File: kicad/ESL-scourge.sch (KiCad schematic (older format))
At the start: 39 parts, among them IC1 MOC3020M, J1 DB9, J2 DB9, P1 CONN_4, P2 CONN_3, P3 CONN_4, Q1 NPN, Q2 NPN, Q3 NPN, U1 TDA2030

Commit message: Comments for debugging added
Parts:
- C6: value 1.0 -> 1.0 x 250V
- D1, D10, D2, D3, D4, D6, D7, D8, D9: value DIODE -> SMA4007 (GS1M)
- Q1, Q2, Q3: value NPN -> BC847
- R10: value R -> 0*
- R8: value R -> 1M*
- R9: value R -> 2k*
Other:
- note added: "*"
- note added: "12V"
- note added: "220V"
- note added: "R1 и R2 подбираются так, чтобы\nАМПЛИТУДНОЕ выходное\nнапряжение менялось в диапазоне\nне менее, чем 20-100 В.\nС помощью осциллографа с\nделителем убедиться, что\nсинус на выходе не срезается."
- note added: "R6=(Vcc-4)/0,015, округляется в\nсторону уменьшения до близжайшего\nдоступного номинала, но не менее,\nчем (Vcc-2)/0,05\n"
- note added: "Если вольтметр на 150В:\nR10 - 0 ом (перемычка)\nR8 - 1M или не монтировать вообще\n(посмотреть, насколько бодро\nвольтметр реагирует на вращение\nрегулятора напряжения)."
- note added: "Здесь важна фазировка обмоток:\nнапряжения должны суммироваться,\nа не вычитаться. Необходимо\nизмерить переменное напряжение\nмежду выводами 1 и 4 P1\n - если там 24 В - все ОК\n - если там около нуля, необходимо\nпоменять местами концы одной из\nвторичных обмоток.\nПредварительно надо убедиться,\nчто на каждой из обмоток есть 12 В."
- note added: "По умолчанию установлен (замкнут)"
- note added: "Посмотреть выходной сигнал\nс отключенным демпфером (R5C5).\nЕсли все ОК - демпфер не ставить."
- note added: "для подбора R9 сделать следующее:\nпри максимальном напряжении на\nвыходе замкнуть контакты 7 и 8\nили лучше замкнуть контакт 8 с\nножкой 6 IC1. Если напряжение на\nвольтметре карабаса уменьшилось\nнезначительно - ОК."
- note added: "может быть заменить на КМОП-логику?"
- note added: "может быть стоит подключить\nвольтметр до резистора тк мб кз\nили предусмотреть индикацию КЗ?"
- note removed: "может быть заменить на КМОП-логику"
- note removed: "может быть стоит подключиться до резистора тк мб кз"
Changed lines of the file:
@@
 Sheet 1 1
 Title ""
-Date "14 feb 2016"
+Date "1 apr 2016"
 Rev ""
 Comp ""
@@
 P 5900 3250
 F 0 "D3" H 5900 3350 40  0000 C CNN
-F 1 "DIODE" H 5900 3150 40  0000 C CNN
+F 1 "SMA4007 (GS1M)" H 5900 3150 40  0000 C CNN
 F 2 "~" H 5900 3250 60  0000 C CNN
 F 3 "~" H 5900 3250 60  0000 C CNN
@@
 P 5900 3850
 F 0 "D4" H 5900 3950 40  0000 C CNN
-F 1 "DIODE" H 5900 3750 40  0000 C CNN
+F 1 "SMA4007 (GS1M)" H 5900 3750 40  0000 C CNN
 F 2 "~" H 5900 3850 60  0000 C CNN
 F 3 "~" H 5900 3850 60  0000 C CNN
@@
 P 8150 2450
 F 0 "C6" H 8150 2550 40  0000 L CNN
-F 1 "1.0" H 8156 2365 40  0000 L CNN
+F 1 "1.0 x 250V" H 8156 2365 40  0000 L CNN
 F 2 "~" H 8188 2300 30  0000 C CNN
 F 3 "~" H 8150 2450 60  0000 C CNN
@@
 P 2700 3000
 F 0 "D1" H 2700 3100 40  0000 C CNN
-F 1 "DIODE" H 2700 2900 40  0000 C CNN
+F 1 "SMA4007 (GS1M)" H 2700 2900 40  0000 C CNN
 F 2 "~" H 2700 3000 60  0000 C CNN
 F 3 "~" H 2700 3000 60  0000 C CNN
@@
 P 2700 3800
 F 0 "D2" H 2700 3900 40  0000 C CNN
-F 1 "DIODE" H 2700 3700 40  0000 C CNN
+F 1 "SMA4007 (GS1M)" H 2700 3700 40  0000 C CNN
 F 2 "~" H 2700 3800 60  0000 C CNN
 F 3 "~" H 2700 3800 60  0000 C CNN
@@
 P 9000 3550
 F 0 "D7" H 9000 3650 40  0000 C CNN
-F 1 "DIODE" H 9000 3450 40  0000 C CNN
+F 1 "SMA4007 (GS1M)" H 9000 3450 40  0000 C CNN
 F 2 "~" H 9000 3550 60  0000 C CNN
 F 3 "~" H 9000 3550 60  0000 C CNN
@@
 P 8300 3550
 F 0 "R9" V 8380 3550 40  0000 C CNN
-F 1 "R" V 8307 3551 40  0000 C CNN
+F 1 "2k*" V 8307 3551 40  0000 C CNN
 F 2 "~" V 8230 3550 30  0000 C CNN
 F 3 "~" H 8300 3550 30  0000 C CNN
@@
 P 9000 4150
 F 0 "D9" H 9000 4250 40  0000 C CNN
-F 1 "DIODE" H 9000 4050 40  0000 C CNN
+F 1 "SMA4007 (GS1M)" H 9000 4050 40  0000 C CNN
 F 2 "~" H 9000 4150 60  0000 C CNN
 F 3 "~" H 9000 4150 60  0000 C CNN
@@
 P 9000 3850
 F 0 "D8" H 9000 3950 40  0000 C CNN
-F 1 "DIODE" H 9000 3750 40  0000 C CNN
+F 1 "SMA4007 (GS1M)" H 9000 3750 40  0000 C CNN
 F 2 "~" H 9000 3850 60  0000 C CNN
 F 3 "~" H 9000 3850 60  0000 C CNN
@@
 P 9000 4450
 F 0 "D10" H 9000 4550 40  0000 C CNN
-F 1 "DIODE" H 9000 4350 40  0000 C CNN
+F 1 "SMA4007 (GS1M)" H 9000 4350 40  0000 C CNN
 F 2 "~" H 9000 4450 60  0000 C CNN
 F 3 "~" H 9000 4450 60  0000 C CNN
@@
 P 8050 5500
 F 0 "Q1" H 8050 5350 50  0000 R CNN
-F 1 "NPN" H 8050 5650 50  0000 R CNN
+F 1 "BC847" H 8050 5650 50  0000 R CNN
 F 2 "~" H 8050 5500 60  0000 C CNN
 F 3 "~" H 8050 5500 60  0000 C CNN
@@
 P 8500 5500
 F 0 "Q2" H 8500 5350 50  0000 R CNN
-F 1 "NPN" H 8500 5650 50  0000 R CNN
+F 1 "BC847" H 8500 5650 50  0000 R CNN
 F 2 "~" H 8500 5500 60  0000 C CNN
 F 3 "~" H 8500 5500 60  0000 C CNN
@@
 P 8850 5700
 F 0 "Q3" H 8850 5550 50  0000 R CNN
-F 1 "NPN" H 8850 5850 50  0000 R CNN
+F 1 "BC847" H 8850 5850 50  0000 R CNN
 F 2 "~" H 8850 5700 60  0000 C CNN
 F 3 "~" H 8850 5700 60  0000 C CNN
@@
 P 8300 3100
 F 0 "D6" H 8300 3200 40  0000 C CNN
-F 1 "DIODE" H 8300 3000 40  0000 C CNN
+F 1 "SMA4007 (GS1M)" H 8300 3000 40  0000 C CNN
 F 2 "~" H 8300 3100 60  0000 C CNN
 F 3 "~" H 8300 3100 60  0000 C CNN
@@
 	1    0    0    -1
 $EndComp
-Text Notes 8400 3300 0    60   ~ 0
-может быть стоит подключиться до резистора тк мб кз
+Text Notes 8850 1500 0    60   ~ 0
+может быть стоит подключить\nвольтметр до резистора тк мб кз\nили предусмотреть индикацию КЗ?
 Text Notes 7450 4950 0    60   ~ 0
 15ма
-Text Notes 5850 5750 0    60   ~ 0
-может быть заменить на КМОП-логику
+Text Notes 9200 5600 0    60   ~ 0
+может быть заменить на КМОП-логику?
 $Comp
 L CONN_4 P1
@@
 P 8550 2200
 F 0 "R10" V 8630 2200 40  0000 C CNN
-F 1 "R" V 8557 2201 40  0000 C CNN
+F 1 "0*" V 8557 2201 40  0000 C CNN
 F 2 "~" V 8480 2200 30  0000 C CNN
 F 3 "~" H 8550 2200 30  0000 C CNN
@@
 P 8200 1950
 F 0 "R8" V 8280 1950 40  0000 C CNN
-F 1 "R" V 8207 1951 40  0000 C CNN
+F 1 "1M*" V 8207 1951 40  0000 C CNN
 F 2 "~" V 8130 1950 30  0000 C CNN
 F 3 "~" H 8200 1950 30  0000 C CNN
@@
 	0    -1   -1   0
 $EndComp
+Text Notes 8550 4850 0    60   ~ 0
+Заменить на db15, сделать совместимым с тредбаном
+Text Notes 1250 3150 0    60   ~ 0
+*
+Text Notes 1250 3550 0    60   ~ 0
+*
 Wire Wire Line
 	4650 3500 4650 3400
@@
 	7800 1500 7800 1650
 Connection ~ 5350 2450
-Text Notes 10250 4000 0    60   ~ 0
-Заменить на db15, сделать совместимым с тредбаном
+Wire Notes Line
+	7550 2400 7500 2450
+Wire Notes Line
+	7500 2450 7550 2500
+Wire Notes Line
+	7550 2500 7500 2550
+Wire Notes Line
+	7500 2550 7550 2600
+Wire Notes Line
+	7550 2600 7500 2650
+Wire Notes Line
+	7500 2650 7550 2700
+Wire Notes Line
+	7550 2700 7700 2700
+Wire Notes Line
+	7550 2400 7800 2400
+Wire Notes Line
+	7350 2400 7400 2450
+Wire Notes Line
+	7400 2450 7350 2500
+Wire Notes Line
+	7350 2500 7400 2550
+Wire Notes Line
+	7400 2550 7350 2600
+Wire Notes Line
+	7350 2600 7400 2650
+Wire Notes Line
+	7400 2650 7350 2700
+Wire Notes Line
+	7350 2700 7200 2700
+Wire Notes Line
+	7100 2400 7350 2400
+Wire Notes Line
+	1250 3050 1200 3100
+Wire Notes Line
+	1200 3100 1250 3150
+Wire Notes Line
+	1250 3150 1200 3200
+Wire Notes Line
+	1200 3200 1250 3250
+Wire Notes Line
+	1250 3250 1200 3300
+Wire Notes Line
+	1200 3300 1250 3350
+Wire Notes Line
+	1250 3350 1650 3350
+Wire Notes Line
+	1250 3050 1550 3050
+Wire Notes Line
+	7450 2400 7450 2700
+Wire Notes Line
+	1050 3250 1100 3300
+Wire Notes Line
+	1100 3300 1050 3350
+Wire Notes Line
+	1050 3350 1100 3400
+Wire Notes Line
+	1100 3400 1050 3450
+Wire Notes Line
+	1050 3450 1100 3500
+Wire Notes Line
+	1100 3500 1050 3550
+Wire Notes Line
+	1050 3550 900  3550
+Wire Notes Line
+	650  3250 1050 3250
+Wire Notes Line
+	1250 3450 1200 3500
+Wire Notes Line
+	1200 3500 1250 3550
+Wire Notes Line
+	1250 3550 1200 3600
+Wire Notes Line
+	1200 3600 1250 3650
+Wire Notes Line
+	1250 3650 1200 3700
+Wire Notes Line
+	1200 3700 1250 3750
+Wire Notes Line
+	1250 3750 1550 3750
+Wire Notes Line
+	1250 3450 1650 3450
+Wire Notes Line
+	1150 3050 1150 3750
+Wire Notes Line
+	7500 2900 7500 2800
+Wire Notes Line
+	7500 2800 7700 2800
+Wire Notes Line
+	7700 2800 7700 2700
+Wire Notes Line
+	7600 2900 7600 2850
+Wire Notes Line
+	7600 2850 7800 2850
+Wire Notes Line
+	7800 2850 7800 2400
+Wire Notes Line
+	7350 2900 7350 2800
+Wire Notes Line
+	7350 2800 7200 2800
+Wire Notes Line
+	7200 2800 7200 2700
+Wire Notes Line
+	7300 2900 7300 2850
+Wire Notes Line
+	7300 2850 7100 2850
+Wire Notes Line
+	7100 2850 7100 2400
+Text Notes 7150 2600 0    60   ~ 0
+12V
+Text Notes 7550 2600 0    60   ~ 0
+220V
+Wire Notes Line
+	1550 3750 1550 3550
+Wire Notes Line
+	1550 3550 1650 3550
+Wire Notes Line
+	1550 3050 1550 3250
+Wire Notes Line
+	1550 3250 1650 3250
+Text Notes 700  1550 0    60   ~ 0
+Здесь важна фазировка обмоток:\nнапряжения должны суммироваться,\nа не вычитаться. Необходимо\nизмерить переменное напряжение\nмежду выводами 1 и 4 P1\n - если там 24 В - все ОК\n - если там около нуля, необходимо\nпоменять местами концы одной из\nвторичных обмоток.\nПредварительно надо убедиться,\nчто на каждой из обмоток есть 12 В.
+Wire Notes Line
+	9700 4750 9900 4550
+Wire Notes Line
+	9900 4550 9900 4600
+Wire Notes Line
+	9900 4550 9850 4550
+Wire Notes Line
+	900  3550 900  4300
+Wire Notes Line
+	850  3800 950  3800
+Wire Notes Line
+	950  3800 950  4000
+Wire Notes Line
+	950  4000 850  4000
+Wire Notes Line
+	850  4000 850  3800
+Wire Notes Line
+	650  3250 650  3800
+Wire Notes Line
+	650  3800 550  4000
+Wire Notes Line
+	650  4000 650  4300
+Wire Notes Line
+	650  4300 700  4250
+Wire Notes Line
+	650  4300 600  4250
+Wire Notes Line
+	900  4300 950  4250
+Wire Notes Line
+	900  4300 850  4250
+Text Notes 650  4500 0    60   ~ 0
+220V
+Text Notes 750  3450 0    60   ~ 0
+220V
+Text Notes 1300 3250 0    60   ~ 0
+12V
+Text Notes 1300 3650 0    60   ~ 0
+12V
+Text Notes 6000 5300 0    60   ~ 0
+R6=(Vcc-4)/0,015, округляется в\nсторону уменьшения до близжайшего\nдоступного номинала, но не менее,\nчем (Vcc-2)/0,05\n
+Text Notes 5600 4950 0    60   ~ 0
+По умолчанию установлен (замкнут)
+Wire Notes Line
+	7150 4350 7250 4300
+Wire Notes Line
+	7250 4300 7200 4400
+Wire Notes Line
+	7250 4300 6650 4850
+Wire Notes Line
+	8700 3250 8400 3450
+Wire Notes Line
+	8400 3450 8450 3450
+Wire Notes Line
+	8400 3450 8400 3400
+Text Notes 8750 2750 0    60   ~ 0
+для подбора R9 сделать следующее:\nпри максимальном напряжении на\nвыходе замкнуть контакты 7 и 8\nили лучше замкнуть контакт 8 с\nножкой 6 IC1. Если напряжение на\nвольтметре карабаса уменьшилось\nнезначительно - ОК.
+Text Notes 8800 1950 0    60   ~ 0
+Если вольтметр на 150В:\nR10 - 0 ом (перемычка)\nR8 - 1M или не монтировать вообще\n(посмотреть, насколько бодро\nвольтметр реагирует на вращение\nрегулятора напряжения).
+Text Notes 2450 4600 0    60   ~ 0
+R1 и R2 подбираются так, чтобы\nАМПЛИТУДНОЕ выходное\nнапряжение менялось в диапазоне\nне менее, чем 20-100 В.\nС помощью осциллографа с\nделителем убедиться, что\nсинус на выходе не срезается.
+Text Notes 5450 1850 0    60   ~ 0
+Посмотреть выходной сигнал\nс отключенным демпфером (R5C5).\nЕсли все ОК - демпфер не ставить.
+Wire Notes Line
+	6600 2150 6650 3400
+Wire Notes Line
+	6650 3400 6700 3250
+Wire Notes Line
+	6650 3400 6600 3250
 $EndSCHEMATC

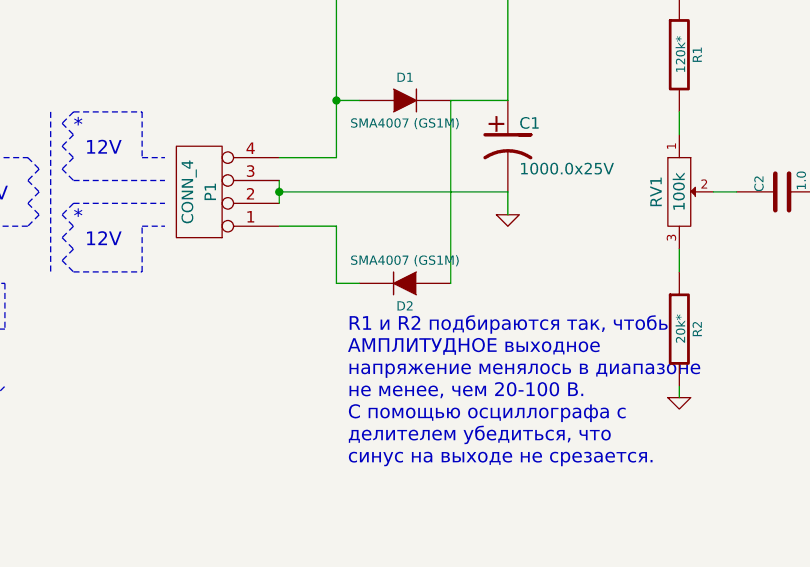
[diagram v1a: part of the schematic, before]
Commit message: Critical bug fixed in power supply circuit - wrong diode polarity
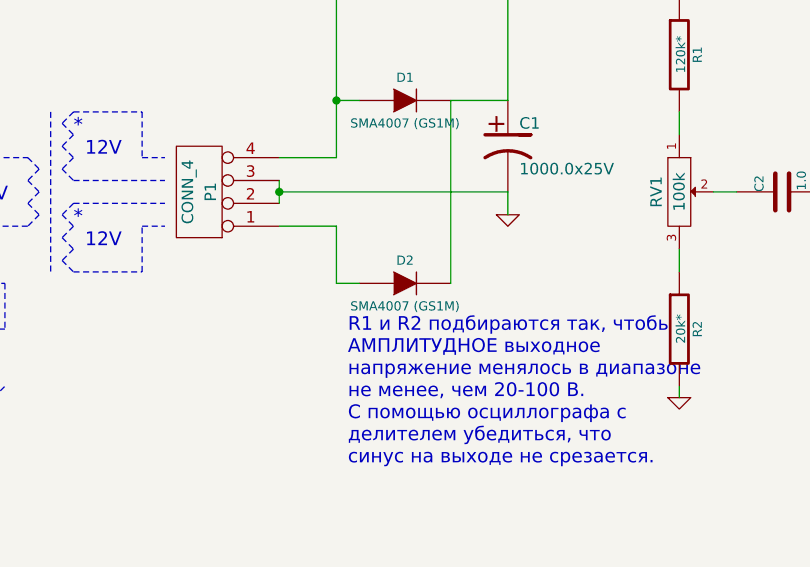
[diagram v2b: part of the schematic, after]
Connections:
- net VCC: now also D2.2 (K); no longer D2.1 (A)
- net at P1.1 (P1): now also D2.1 (A); no longer D2.2 (K)
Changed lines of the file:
@@
 Sheet 1 1
 Title ""
-Date "1 apr 2016"
+Date "2 apr 2016"
 Rev ""
 Comp ""
@@
 F 3 "~" H 2700 3800 60  0000 C CNN
 	1    2700 3800
-	-1   0    0    1
-$EndComp
-$Comp
+	1    0    0    -1
+$EndComp
+$Comp

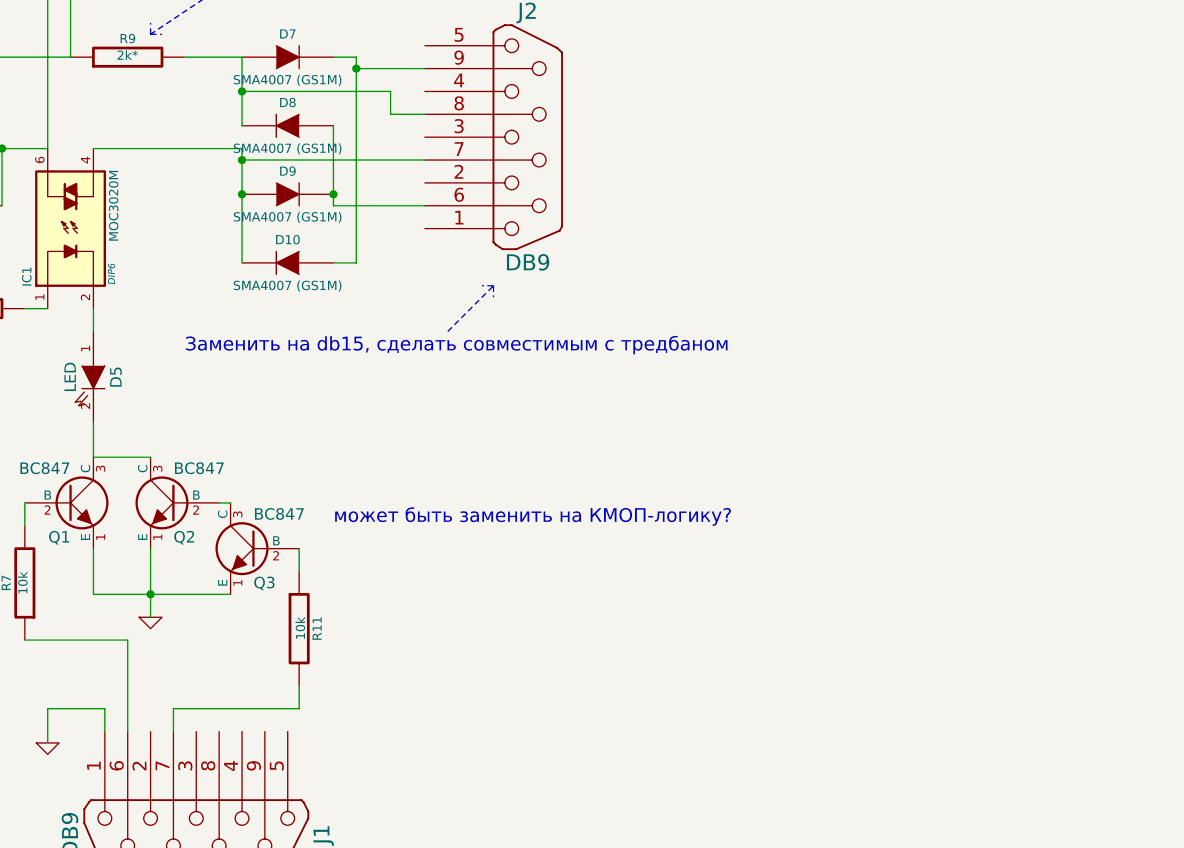
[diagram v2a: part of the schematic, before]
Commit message: Several critical bugs fixed - wrong diode polarity in output bridge, pullup resistors added in slon-control scheme
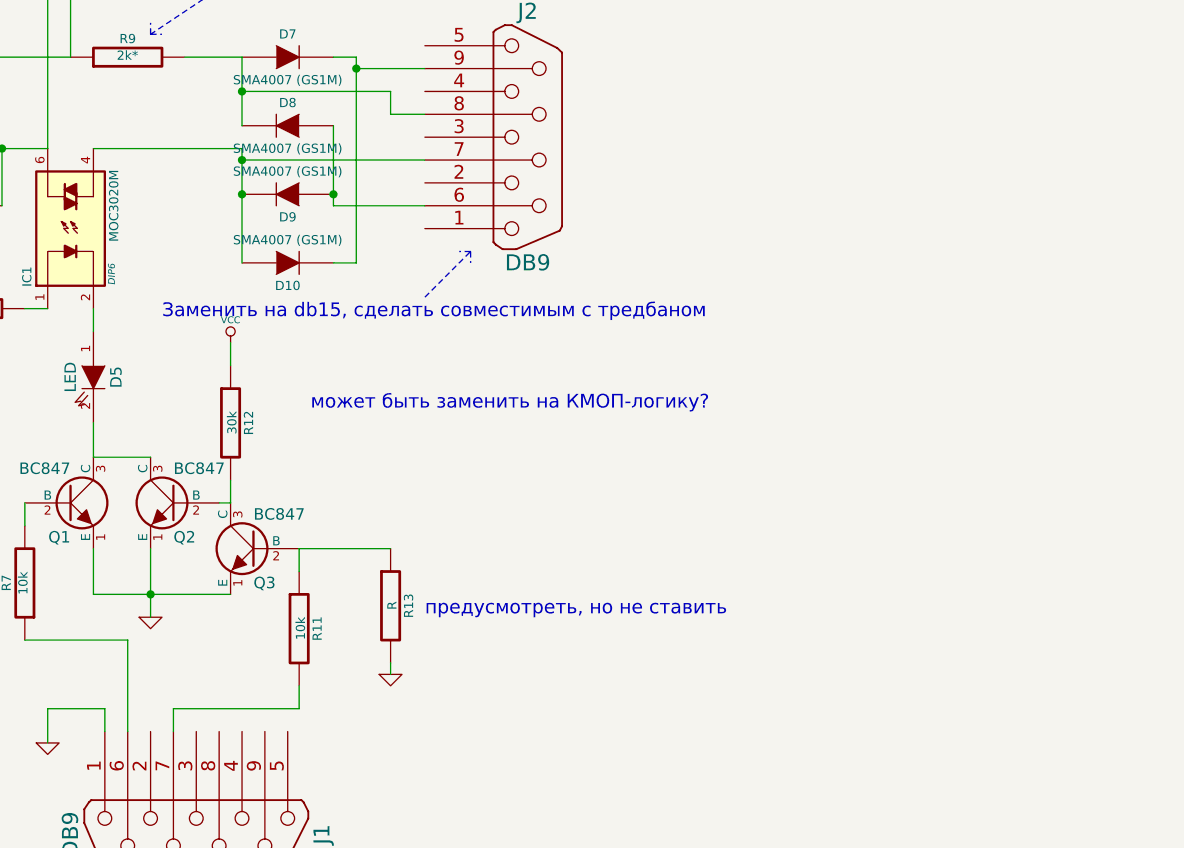
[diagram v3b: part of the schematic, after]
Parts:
- added R12: 30k, ~, symbol R
- added R13: R, ~, symbol R
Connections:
- net GND: now also R13.2
- net VCC: now also R12.1
- net at IC1.4, J2.7 (P7): now also D10.1 (A), D9.2 (K); no longer D10.2 (K), D9.1 (A)
- net at D7.2 (K), J2.9 (P9): now also D10.2 (K); no longer D10.1 (A)
- net at D8.1 (A), J2.6 (P6): now also D9.1 (A); no longer D9.2 (K)
- net at Q2.2 (B), Q3.3 (C): now also R12.2
- net at Q3.2 (B), R11.1: now also R13.1
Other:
- note added: "предусмотреть, но не ставить"
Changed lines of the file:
@@
 Sheet 1 1
 Title ""
-Date "2 apr 2016"
+Date "11 apr 2016"
 Rev ""
 Comp ""
@@
 F 3 "~" H 9000 4150 60  0000 C CNN
 	1    9000 4150
-	1    0    0    -1
+	-1   0    0    1
 $EndComp
 $Comp
@@
 F 3 "~" H 9000 4450 60  0000 C CNN
 	1    9000 4450
-	-1   0    0    -1
+	1    0    0    1
 $EndComp
 $Comp
@@
 Text Notes 7450 4950 0    60   ~ 0
 15ма
-Text Notes 9200 5600 0    60   ~ 0
+Text Notes 9100 5100 0    60   ~ 0
 может быть заменить на КМОП-логику?
 $Comp
@@
 	0    -1   -1   0
 $EndComp
-Text Notes 8550 4850 0    60   ~ 0
+Text Notes 8450 4700 0    60   ~ 0
 Заменить на db15, сделать совместимым с тредбаном
 Text Notes 1250 3150 0    60   ~ 0
@@
 Здесь важна фазировка обмоток:\nнапряжения должны суммироваться,\nа не вычитаться. Необходимо\nизмерить переменное напряжение\nмежду выводами 1 и 4 P1\n - если там 24 В - все ОК\n - если там около нуля, необходимо\nпоменять местами концы одной из\nвторичных обмоток.\nПредварительно надо убедиться,\nчто на каждой из обмоток есть 12 В.
 Wire Notes Line
-	9700 4750 9900 4550
-Wire Notes Line
-	9900 4550 9900 4600
-Wire Notes Line
-	9900 4550 9850 4550
+	9600 4600 9800 4400
+Wire Notes Line
+	9800 4400 9800 4450
+Wire Notes Line
+	9800 4400 9750 4400
 Wire Notes Line
 	900  3550 900  4300
@@
 Wire Notes Line
 	6650 3400 6600 3250
+$Comp
+L R R12
+U 1 1 570BF5CA
+P 8750 5150
+F 0 "R12" V 8830 5150 40  0000 C CNN
+F 1 "30k" V 8757 5151 40  0000 C CNN
+F 2 "~" V 8680 5150 30  0000 C CNN
+F 3 "~" H 8750 5150 30  0000 C CNN
+	1    8750 5150
+	1    0    0    -1
+$EndComp
+$Comp
+L VCC #PWR012
+U 1 1 570BF5E1
+P 8750 4800
+F 0 "#PWR012" H 8750 4900 30  0001 C CNN
+F 1 "VCC" H 8750 4900 30  0000 C CNN
+F 2 "" H 8750 4800 60  0000 C CNN
+F 3 "" H 8750 4800 60  0000 C CNN
+	1    8750 4800
+	1    0    0    -1
+$EndComp
+Wire Wire Line
+	8750 4800 8750 4900
+Wire Wire Line
+	8750 5500 8750 5400
+$Comp
+L R R13
+U 1 1 570BF83C
+P 9450 5950
+F 0 "R13" V 9530 5950 40  0000 C CNN
+F 1 "R" V 9457 5951 40  0000 C CNN
+F 2 "~" V 9380 5950 30  0000 C CNN
+F 3 "~" H 9450 5950 30  0000 C CNN
+	1    9450 5950
+	1    0    0    -1
+$EndComp
+Wire Wire Line
+	9050 5700 9450 5700
+$Comp
+L GND #PWR013
+U 1 1 570BF910
+P 9450 6250
+F 0 "#PWR013" H 9450 6250 30  0001 C CNN
+F 1 "GND" H 9450 6180 30  0001 C CNN
+F 2 "" H 9450 6250 60  0000 C CNN
+F 3 "" H 9450 6250 60  0000 C CNN
+	1    9450 6250
+	1    0    0    -1
+$EndComp
+Wire Wire Line
+	9450 6200 9450 6250
+Text Notes 9600 6000 0    60   ~ 0
+предусмотреть, но не ставить
 $EndSCHEMATC

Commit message: component values corrected. Work in progress
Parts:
- added C? (x2): 22x350 12-18mm, ~, symbol CP1
- added D?: SMA4007 (GS1M), ~, symbol DIODE
- added RV?: SH-855MC, 100k, ~, symbol POT
- C1: value 1000.0x25V -> 1000.0x35V 13mm
- C4: value 2200.0x25V -> 2200.0x35V 16-18mm
- R13: value R -> 30k
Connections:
- net at IC1.6, JP1.1, P2.1 (P1)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: now also D6.1 (A), C?.2; no longer C6.1
- net at P3.4 (P4), R9.1: now also C?.2; no longer D6.1 (A)
- new net: C?.1, D6.2 (K), D?.1 (A)
- new net: C?.1, D?.2 (K)
- now unconnected: C6.2, R10.2
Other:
- note added: "ТТП-30 (2х18В, 0.75А)\n(лучше ТТП-15 2х18В, но его не найти)"
- note added: "Торэл ТТП-3 (12В, 0.2А)"
- moved on the sheet: C6, D6
